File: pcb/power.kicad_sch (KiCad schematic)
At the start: 58 parts, among them Q1 AO3400_C181090, Q2 AO3401A, U1 F1C200s, U2 TP5400, U3 09.0103_XC6206, U4 09.0102_EA3036

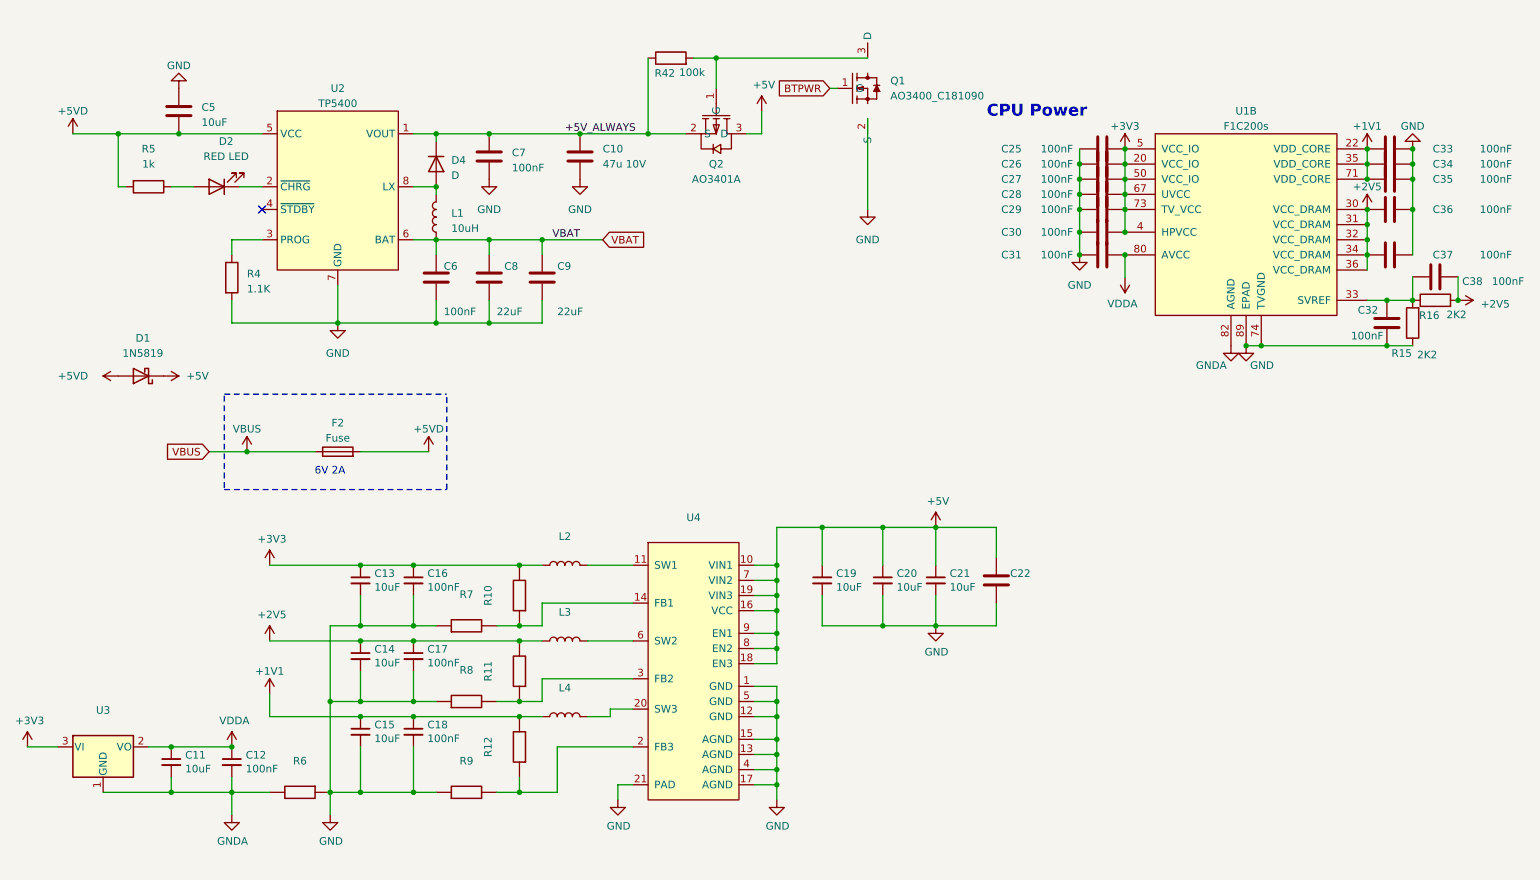
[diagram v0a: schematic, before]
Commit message: Added last minor patches like ideal diode on PCB, added backplate
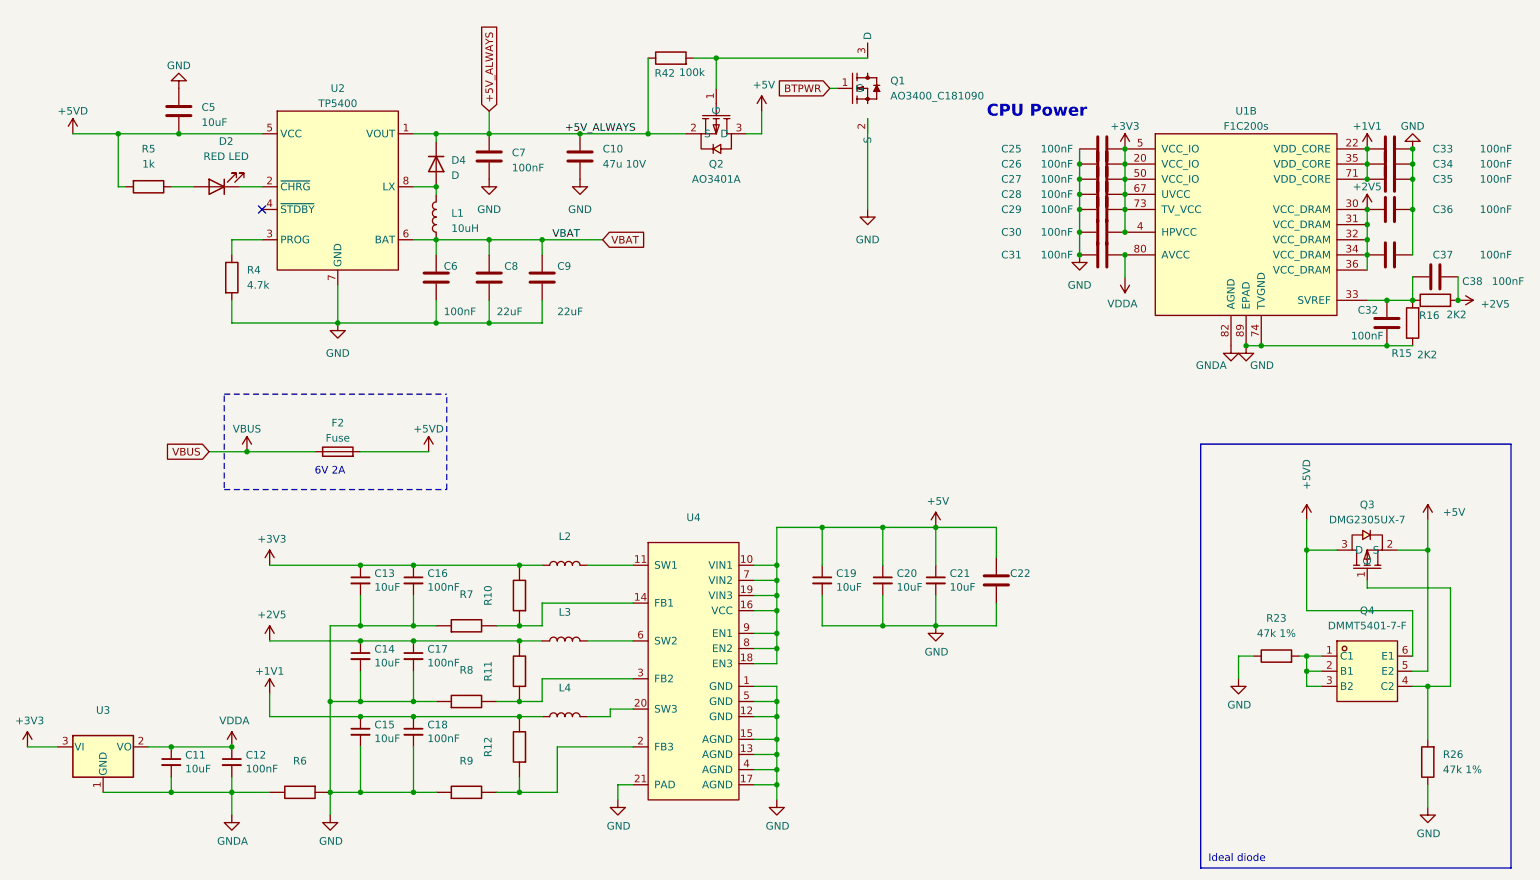
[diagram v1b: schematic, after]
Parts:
- removed D1: 1N5819, Diode_SMD:D_SOD-123, symbol Diode:1N5819
- added Q3: DMG2305UX-7, lcsc:SOT-23-3_L2.9-W1.3-P1.90-LS2.4-BR, symbol lcsc:DMG2305UX-7
- added Q4: DMMT5401-7-F, lcsc:SOT-23-6_L2.9-W1.6-P0.95-LS2.8-BR, symbol lcsc:DMMT5401-7-F
- added R23, R26: 47k 1%, Resistor_SMD:R_0402_1005Metric, symbol Device:R
- R4: value 1.1K -> 4.7k
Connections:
- net +5V: now also Q3.2 (S), Q4.5 (E2)
- net +5VD: now also Q3.3 (D), Q4.6 (E1)
- net GND: now also R23.1, R26.1
- new net: Q4.1 (C1), Q4.2 (B1), Q4.3 (B2), R23.2
- new net: Q3.1 (G), Q4.4 (C2), R26.2
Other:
- note added: "Ideal diode"
